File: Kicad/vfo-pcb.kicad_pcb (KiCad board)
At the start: 2 copper layers, 108.3 x 82.9 mm, 66 parts, among them J10 Link-out 1a, J11 RxTx, J13 Link-out 1b, J14 V12, J17 Link-out 2a, J18 Link-out 3, J19 Link-out 2b, J2 Conn_01x07_Female, J3 Si5351, J4 ESP32L, J5 ESP32R, J6 Rotery Encoder1, J7 ILI9341, J8 Rotery Encoder2, J9 Analog in 3-6, SW1 Rotary_Encoder_Switch, U1 AS179-92LF, U2 74HC595, U3 L7805, U4 AS179-92LF

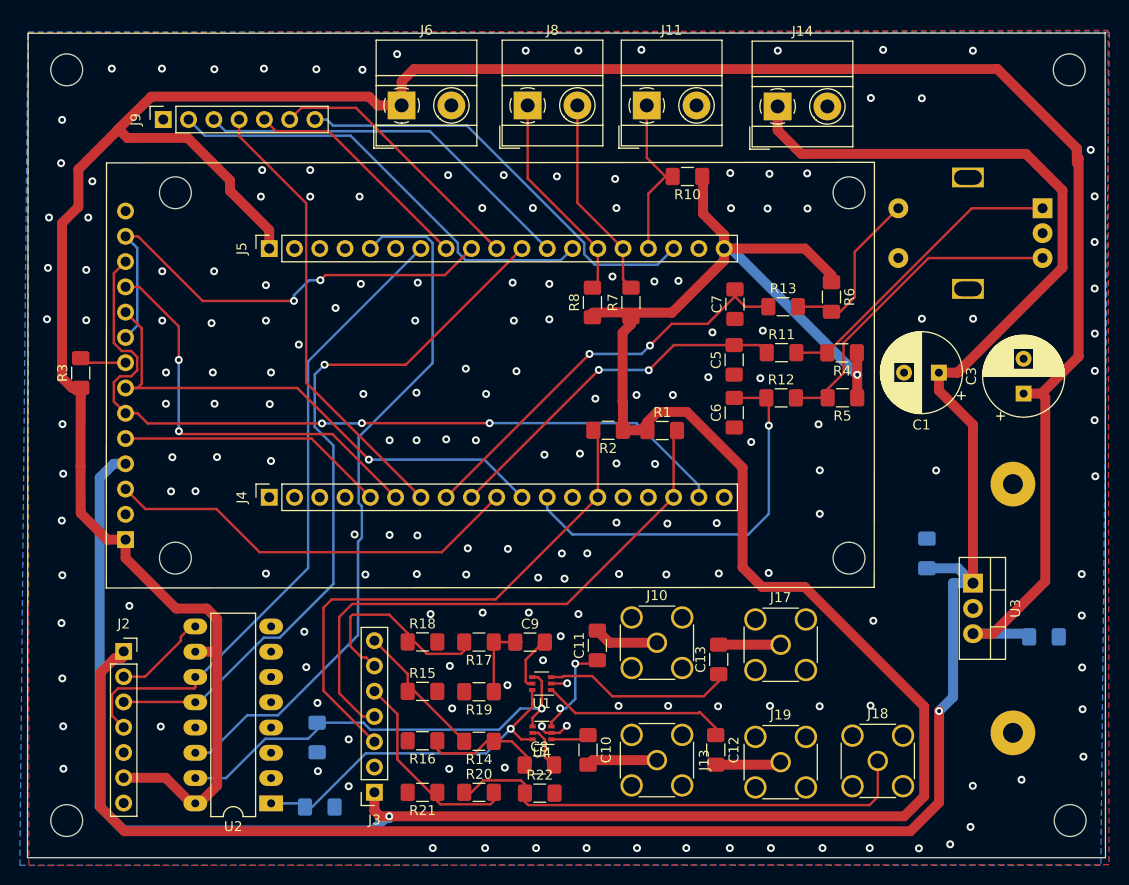
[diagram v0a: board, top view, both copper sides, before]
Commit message: Attenuator removed
To improve crosstalk the attenuators are removed and replaced by 100nF DC blocker
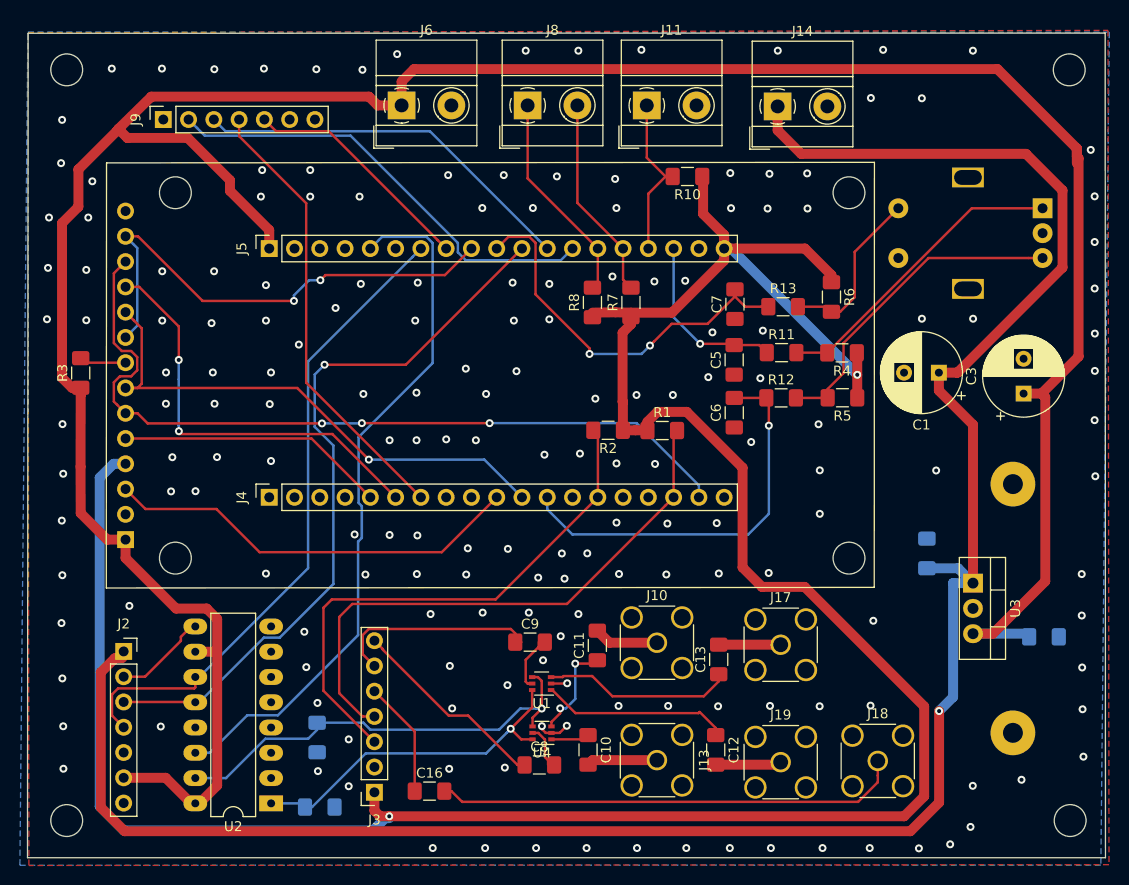
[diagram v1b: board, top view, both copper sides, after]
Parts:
- removed R14, R17, R20: 71, Resistor_SMD:R_1206_3216Metric_Pad1.42x1.75mm_HandSolder
- removed R15, R16, R18, R19, R21, R22: 100, Resistor_SMD:R_1206_3216Metric_Pad1.42x1.75mm_HandSolder
- added C16: 100n, Capacitor_SMD:C_1206_3216Metric_Pad1.42x1.75mm_HandSolder, F.Cu at (82.7, 128.5)
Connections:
- C8 pad 1: Net-(C8-Pad1) -> I3_1
- C9 pad 1: Net-(C9-Pad1) -> I2_1
- J4 pad 8: R3_2a -> Net-(J4-Pad8)
- J4 pad 9: R1_2a -> Net-(J4-Pad9)
- J5 pad 10: A5P -> R3_2a
- J5 pad 17: A6P -> R1_2a
- J9 pad 6: A5P -> Net-(J9-Pad6)
- J9 pad 7: A6P -> Net-(J9-Pad7)
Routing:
- net A6P: track 43.4 -> 0.00 mm
- net A5P: track 27.2 -> 0.00 mm
- net R1_2a: track 36.4 -> 17.7 mm, vias 2 -> 1
- net Net-(C8-Pad1): track 12.2 -> 0.00 mm
- net I1_1: track 20.9 -> 11.7 mm
- net Net-(C9-Pad1): track 7.76 -> 0.00 mm
- net I3_1: track 14.3 -> 20.3 mm
- net R3_2a: track 41.9 -> 39.5 mm
- net Net-(C16-Pad2): track 48.1 -> 47.0 mm
- net I2_1: track 20.9 -> 20.2 mm

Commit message: Add files via upload
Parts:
- removed J17: Link-out 2a, Connector_Coaxial:SMA_Amphenol_132134_Vertical
- removed J18: Link-out 3, Connector_Coaxial:SMA_Amphenol_132134_Vertical
- removed J19: Link-out 2b, Connector_Coaxial:SMA_Amphenol_132134_Vertical
- removed the J9 at (56.0, 61.0)
- removed the U1 at (94.0, 117.7)
- added C17: 100n, Capacitor_SMD:C_1206_3216Metric_Pad1.42x1.75mm_HandSolder, F.Cu at (65.2, 84.3)
- added C18: 100n, Capacitor_SMD:C_1206_3216Metric_Pad1.42x1.75mm_HandSolder, F.Cu at (99.8, 116.3)
- added C19: 100n, Capacitor_SMD:C_1206_3216Metric_Pad1.42x1.75mm_HandSolder, F.Cu at (57.6, 115.9)
- added C20: 100n, Capacitor_SMD:C_1206_3216Metric_Pad1.42x1.75mm_HandSolder, F.Cu at (76.1, 126.2)
- added C21: 100n, Capacitor_SMD:C_1206_3216Metric_Pad1.42x1.75mm_HandSolder, F.Cu at (117.5, 125.9)
- added C22: 100n, Capacitor_SMD:C_1206_3216Metric_Pad1.42x1.75mm_HandSolder, F.Cu at (63.0, 126.0)
- added C23: 100n, Capacitor_SMD:C_1206_3216Metric_Pad1.42x1.75mm_HandSolder, F.Cu at (103.5, 125.9)
- added J11: Link-out 1-1, Connector_Coaxial:SMA_Amphenol_132134_Vertical, F.Cu at (110.9, 127.6)
- added J12: Link-out 1-2, Connector_Coaxial:SMA_Amphenol_132134_Vertical, F.Cu at (97.6, 127.6)
- added J14: Link-out 2-1, Connector_Coaxial:SMA_Amphenol_132134_Vertical, F.Cu at (69.6, 127.6)
- added J15: Link-out 2-2, Connector_Coaxial:SMA_Amphenol_132134_Vertical, F.Cu at (56.2, 127.6)
- added Q1: BFR92, Package_TO_SOT_SMD:SOT-323_SC-70, F.Cu at (75.9, 121.0)
- added Q2: BFR92, Package_TO_SOT_SMD:SOT-323_SC-70, F.Cu at (59.3, 121.7)
- added Q3: BFR92, Package_TO_SOT_SMD:SOT-323_SC-70, F.Cu at (67.6, 117.0)
- added Q4: BFR92, Package_TO_SOT_SMD:SOT-323_SC-70, F.Cu at (120.8, 121.0)
- added Q5: BFR92, Package_TO_SOT_SMD:SOT-323_SC-70, F.Cu at (100.5, 120.7)
- added Q6: BFR92, Package_TO_SOT_SMD:SOT-323_SC-70, F.Cu at (115.3, 121.1)
- added R13: 2.2k, Resistor_SMD:R_1206_3216Metric_Pad1.42x1.75mm_HandSolder, F.Cu at (76.3, 104.4)
- added R14: 2.2k, Resistor_SMD:R_1206_3216Metric_Pad1.42x1.75mm_HandSolder, F.Cu at (69.7, 104.4)
- added R15: 1k, Resistor_SMD:R_1206_3216Metric_Pad1.42x1.75mm_HandSolder, F.Cu at (73.6, 110.0)
- added R16: 1k, Resistor_SMD:R_1206_3216Metric_Pad1.42x1.75mm_HandSolder, F.Cu at (66.5, 112.3)
- added R17: 1k, Resistor_SMD:R_1206_3216Metric_Pad1.42x1.75mm_HandSolder, F.Cu at (60.1, 119.1)
- added R18: 47, Resistor_SMD:R_1206_3216Metric_Pad1.42x1.75mm_HandSolder, F.Cu at (78.4, 116.7)
- added R19: 47, Resistor_SMD:R_1206_3216Metric_Pad1.42x1.75mm_HandSolder, F.Cu at (54.5, 119.4)
- added R20: 47, Resistor_SMD:R_1206_3216Metric_Pad1.42x1.75mm_HandSolder, F.Cu at (64.0, 117.3)
- added R21: 1k, Resistor_SMD:R_1206_3216Metric_Pad1.42x1.75mm_HandSolder, F.Cu at (117.8, 112.7)
- added R22: 1k, Resistor_SMD:R_1206_3216Metric_Pad1.42x1.75mm_HandSolder, F.Cu at (113.2, 112.7)
- added R23: 1k, Resistor_SMD:R_1206_3216Metric_Pad1.42x1.75mm_HandSolder, F.Cu at (108.5, 115.6)
- added R24: 47, Resistor_SMD:R_1206_3216Metric_Pad1.42x1.75mm_HandSolder, F.Cu at (126.1, 115.9)
- added R25: 47, Resistor_SMD:R_1206_3216Metric_Pad1.42x1.75mm_HandSolder, F.Cu at (95.1, 117.6)
- added R26: 47, Resistor_SMD:R_1206_3216Metric_Pad1.42x1.75mm_HandSolder, F.Cu at (110.1, 118.8)
- added U3: Si5351A-B-GT, Package_SO:MSOP-10_3x3mm_P0.5mm, F.Cu at (59.9, 112.7)
- added Y1: Crystal, Crystal:Crystal_SMD_TXC_7M-4Pin_3.2x2.5mm_HandSoldering, F.Cu at (97.4, 110.4)
- added Y2: Crystal, Crystal:Crystal_SMD_TXC_7M-4Pin_3.2x2.5mm_HandSoldering, F.Cu at (50.6, 114.6)
- C14, C15: moved to F.Cu
- C16: value 100n -> 10u
- J10: value Link-out 1a -> Link-out 1-0
- J13: value Link-out 1b -> Link-out 2-0
- J3: value Si5351 -> Analog in 3-6
- R6: renamed from R3; moved to B.Cu
- U2: value 74HC595 -> Si5351A-B-GT; footprint Package_DIP:DIP-16_W7.62mm_LongPads -> Package_SO:MSOP-10_3x3mm_P0.5mm
- U4: value AS179-92LF -> AMS1117; footprint Package_TO_SOT_SMD:SOT-363_SC-70-6 -> Package_TO_SOT_SMD:SOT-223-3_TabPin2
- moved J3 59.7 mm to (74.8, 69.0), turned to 90 degrees
- moved J9 52.7 mm to (57.7, 62.0), turned to 90 degrees
- moved C16 51.7 mm to (65.2, 79.8), turned to 180 degrees
- moved U4 44.3 mm to (63.6, 90.4), turned to 0 degrees
- moved C13 44.1 mm to (68.0, 121.0), turned to 0 degrees
- moved U2 42.1 mm to (104.8, 111.7), turned to 0 degrees
- moved C9 40.4 mm to (52.5, 110.2)
- moved C10 27.7 mm to (126.1, 120.4), turned to 0 degrees
- moved J13 22.7 mm to (83.0, 127.6), turned to 0 degrees
- moved J10 22.6 mm to (123.3, 127.6)
- moved C8 21.1 mm to (102.6, 106.7), turned to 270 degrees
- moved C15 17.0 mm to (54.5, 122.0), turned to 180 degrees
- moved C12 16.7 mm to (95.1, 120.8), turned to 180 degrees
- moved C14 13.3 mm to (81.5, 121.1)
- moved C11 13.2 mm to (110.0, 121.9), turned to 180 degrees
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- renumbered C5 to C3, C3 to C4, C6 to C5, C4 to C6, J6 to J1, J8 to J2, J11 to J4, J14 to J5, J4 to J6, J5 to J7, J7 to J8, J2 to J9, R7 to R1, R12 to R10, R6 to R11, R13 to R12, R8 to R2, R10 to R3, R1 to R4, R2 to R5, R4 to R7, R11 to R8, R5 to R9, U3 to U1
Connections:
- C14 pad 1: Qb -> Net-(C14-Pad1)
- C14 pad 2: GND -> Net-(C14-Pad2)
- C15 pad 1: Qa -> Net-(C15-Pad1)
- C15 pad 2: GND -> Net-(C15-Pad2)
- C16 pad 1: I1_1 -> V33a
- C16 pad 2: Net-(C16-Pad2) -> GND
- C8 pad 1: I3_1 -> GND
- C8 pad 2: Net-(C8-Pad2) -> V33a
- C9 pad 1: I2_1 -> GND
- C9 pad 2: Net-(C9-Pad2) -> V33a
- J10 pad 1: Net-(C11-Pad2) -> Net-(C10-Pad2)
- J13 pad 1: Net-(C10-Pad2) -> Net-(C14-Pad2)
- J3 pad 1: V33 -> GND
- J3 pad 2: GND -> A1P
- J3 pad 3: SDA_1 -> A2P
- J3 pad 4: SCL_1 -> A3P
- J3 pad 5: I1_1 -> A4P
- J3 pad 6: I2_1 -> Net-(J3-Pad6)
- J3 pad 7: I3_1 -> Net-(J3-Pad7)
- J6 pad 8: Net-(J4-Pad8) -> SDA_2
- J6 pad 9: Net-(J4-Pad9) -> SCL_2
- J8 pad 4: V33 -> V33a
- J9 pad 2: Dout -> SER_2
- U2 pad 1: Qb -> V33a
- U2 pad 10: Vcc -> Net-(R21-Pad2)
- U2 pad 4: Net-(U2-Pad4) -> SCL_1
- U2 pad 5: Net-(U2-Pad5) -> SDA_1
- U2 pad 7: Net-(U2-Pad7) -> V33a
- U2 pad 9: Dout -> Net-(R22-Pad2)
- U4 pad 1: Net-(C10-Pad1) -> GND
- U4 pad 2: GND -> V33a
- U4 pad 3: Net-(C11-Pad1) -> Vcc
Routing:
- net V33a: track 0.00 -> 292.4 mm, vias 0 -> 4
- net V33: track 256.9 -> 75.6 mm, vias 2 -> 1
- net V12V: track 214.0 -> 150.4 mm, vias 1 -> 0
- net SER_2: track 71.0 -> 21.5 mm
- net SCL_2: track 0.00 -> 48.0 mm, vias 0 -> 1
- net Net-(C16-Pad2): track 47.0 -> 0.00 mm
- net Qa: track 44.8 -> 0.00 mm, vias 1 -> 0
- net SCLK_2: track 66.2 -> 21.5 mm
- net RCLK_2: track 73.9 -> 35.7 mm, vias 1 -> 0
- net SDA_2: track 0.00 -> 37.4 mm, vias 0 -> 1
- net Qb: track 34.9 -> 0.00 mm, vias 1 -> 0
- net SCL_1: track 57.6 -> 23.2 mm
- net A1P: track 45.5 -> 24.2 mm
- net I3_1: track 20.3 -> 0.00 mm
- net I2_1: track 20.2 -> 0.00 mm
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
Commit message: Add files via upload
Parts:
- removed C10, C11, C12, C13, C14, C15: 100n, Capacitor_SMD:C_1206_3216Metric_Pad1.42x1.75mm_HandSolder
- Q1, Q2, Q3, Q4, Q5, Q6: footprint Package_TO_SOT_SMD:SOT-323_SC-70 -> Package_TO_SOT_SMD:SOT-23
- R18, R19, R20, R24, R25: value 47 -> 20
- moved R20 6.01 mm to (68.1, 121.7), turned to 0 degrees
- moved R18 5.88 mm to (81.5, 121.7), turned to 0 degrees
- moved R24 5.84 mm to (125.9, 121.8), turned to 0 degrees
- moved R25 4.02 mm to (95.5, 121.6), turned to 180 degrees
- moved R26 3.25 mm to (110.4, 122.1), turned to 180 degrees
- moved R19 1.70 mm to (54.2, 121.1), turned to 270 degrees
- moved J15 0.70 mm to (56.1, 128.3)
- moved J10 0.70 mm to (123.3, 128.3)
- moved J11 0.70 mm to (110.9, 128.3)
- moved J12 0.70 mm to (97.6, 128.3)
- moved J13 0.70 mm to (83.0, 128.3)
- moved J14 0.70 mm to (69.6, 128.3)
- moved R17 0.64 mm to (59.8, 118.5)
- moved Y2 0.57 mm to (50.7, 115.1), turned to 180 degrees
- moved Y1 0.41 mm to (97.7, 110.6), turned to 180 degrees
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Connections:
- J10 pad 1: Net-(C10-Pad2) -> Net-(J10-Pad1)
- J11 pad 1: Net-(C11-Pad2) -> Net-(J11-Pad1)
- J12 pad 1: Net-(C12-Pad2) -> Net-(J12-Pad1)
- J13 pad 1: Net-(C14-Pad2) -> Net-(J13-Pad1)
- J14 pad 1: Net-(C13-Pad2) -> Net-(J14-Pad1)
- J15 pad 1: Net-(C15-Pad2) -> Net-(J15-Pad1)
- Q1 pad 2: Net-(C14-Pad1) -> Net-(Q1-Pad2)
- Q2 pad 2: Net-(C15-Pad1) -> Net-(Q2-Pad2)
- Q3 pad 2: Net-(C13-Pad1) -> Net-(Q3-Pad2)
- Q4 pad 2: Net-(C10-Pad1) -> Net-(Q4-Pad2)
- Q5 pad 2: Net-(C12-Pad1) -> Net-(Q5-Pad2)
- Q6 pad 2: Net-(C11-Pad1) -> Net-(Q6-Pad2)
- R18 pad 1: GND -> Net-(Q1-Pad2)
- R18 pad 2: Net-(C14-Pad1) -> Net-(J13-Pad1)
- R19 pad 1: GND -> Net-(Q2-Pad2)
- R19 pad 2: Net-(C15-Pad1) -> Net-(J15-Pad1)
- R20 pad 1: GND -> Net-(Q3-Pad2)
- R20 pad 2: Net-(C13-Pad1) -> Net-(J14-Pad1)
- R24 pad 1: GND -> Net-(Q4-Pad2)
- R24 pad 2: Net-(C10-Pad1) -> Net-(J10-Pad1)
- R25 pad 1: GND -> Net-(Q5-Pad2)
- R25 pad 2: Net-(C12-Pad1) -> Net-(J12-Pad1)
- R26 pad 1: GND -> Net-(Q6-Pad2)
- R26 pad 2: Net-(C11-Pad1) -> Net-(J11-Pad1)
- Y1 pad 1: Net-(U2-Pad3) -> Net-(U2-Pad2)
- Y1 pad 2: Net-(U2-Pad2) -> GND
- Y1 pad 3: (no net) -> Net-(U2-Pad3)
- Y2 pad 1: Net-(U3-Pad3) -> Net-(U3-Pad2)
- Y2 pad 2: Net-(U3-Pad2) -> GND
- Y2 pad 3: (no net) -> Net-(U3-Pad3)
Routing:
- net Net-(C13-Pad1): track 9.76 -> 0.00 mm
- net Net-(C10-Pad2): track 9.61 -> 0.00 mm
- net Net-(C12-Pad2): track 9.10 -> 0.00 mm
- net Net-(J10-Pad1): track 0.00 -> 8.66 mm
- net Net-(J12-Pad1): track 0.00 -> 8.61 mm
- net Net-(J11-Pad1): track 0.00 -> 7.45 mm
- net Net-(C15-Pad2): track 7.33 -> 0.00 mm
- net Net-(C10-Pad1): track 7.26 -> 0.00 mm
- net Net-(C14-Pad1): track 7.04 -> 0.00 mm
- net Net-(C11-Pad2): track 6.68 -> 0.00 mm
- net Net-(C13-Pad2): track 6.63 -> 0.00 mm
- net Net-(J14-Pad1): track 0.00 -> 6.62 mm
- net Net-(J13-Pad1): track 0.00 -> 6.60 mm
- net Net-(C12-Pad1): track 6.59 -> 0.00 mm
- net Net-(J15-Pad1): track 0.00 -> 6.51 mm
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
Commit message: Add files via upload
Updated output circuit added pi attenuation
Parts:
- added R19: 1k, Resistor_SMD:R_1206_3216Metric_Pad1.42x1.75mm_HandSolder, F.Cu at (114.8, 112.6)
- added R21: 150, Resistor_SMD:R_1206_3216Metric_Pad1.42x1.75mm_HandSolder, F.Cu at (81.5, 117.7)
- added R23: 150, Resistor_SMD:R_1206_3216Metric_Pad1.42x1.75mm_HandSolder, F.Cu at (124.5, 113.0)
- added R24: 150, Resistor_SMD:R_1206_3216Metric_Pad1.42x1.75mm_HandSolder, F.Cu at (100.9, 118.9)
- added R25: 150, Resistor_SMD:R_1206_3216Metric_Pad1.42x1.75mm_HandSolder, F.Cu at (67.1, 119.3)
- added R29: 150, Resistor_SMD:R_1206_3216Metric_Pad1.42x1.75mm_HandSolder, F.Cu at (108.2, 118.6)
- added R32: 150, Resistor_SMD:R_1206_3216Metric_Pad1.42x1.75mm_HandSolder, F.Cu at (127.5, 118.7)
- added R33: 150, Resistor_SMD:R_1206_3216Metric_Pad1.42x1.75mm_HandSolder, F.Cu at (81.5, 114.3)
- added R34: 150, Resistor_SMD:R_1206_3216Metric_Pad1.42x1.75mm_HandSolder, F.Cu at (63.2, 128.3)
- added R36: 150, Resistor_SMD:R_1206_3216Metric_Pad1.42x1.75mm_HandSolder, F.Cu at (102.5, 124.0)
- added R37: 150, Resistor_SMD:R_1206_3216Metric_Pad1.42x1.75mm_HandSolder, F.Cu at (76.3, 127.2)
- added R38: 150, Resistor_SMD:R_1206_3216Metric_Pad1.42x1.75mm_HandSolder, F.Cu at (105.6, 124.0)
- R22: value 1k -> 150
- R26: renamed from R18; value 20 -> 33
- R27: renamed from R19; value 20 -> 33
- R28: renamed from R24; value 20 -> 33
- R30: renamed from R25; value 20 -> 33
- R31: renamed from R20; value 20 -> 33
- R35: renamed from R26; value 47 -> 33
- moved R22 65.9 mm to (47.8, 120.1), turned to 270 degrees
- moved C7 20.4 mm to (86.7, 114.3), turned to 0 degrees
- moved C16 13.0 mm to (112.2, 112.6)
- moved R20 7.52 mm to (100.9, 116.1)
- moved R26 6.54 mm to (86.7, 117.7)
- moved Q4 6.04 mm to (95.6, 117.0)
- moved C3 5.29 mm to (77.1, 121.0)
- moved Q1 4.95 mm to (75.0, 116.1)
- moved R31 4.76 mm to (72.3, 119.4)
- moved R30 4.54 mm to (91.4, 119.6), turned to 270 degrees
- moved R27 3.98 mm to (50.4, 120.1)
- moved R35 3.54 mm to (111.2, 118.6), turned to 270 degrees
- moved R17 3.54 mm to (63.2, 117.4), turned to 90 degrees
- moved R28 3.40 mm to (124.7, 118.6), turned to 270 degrees
- moved   3.12 mm to (46.0, 128.4)
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- renumbered C16 to C1, C4 to C10, C5 to C11, C6 to C12, C7 to C13, C9 to C14, C8 to C15, C18 to C16, C19 to C17, C17 to C2, C20 to C3, C21 to C4, C22 to C5, C1 to C6, C23 to C7, C2 to C8, C3 to C9, J12 to J10, J10 to J11, J13 to J12, J15 to J13, J11 to J15, Q4 to Q3, Q5 to Q4, Q3 to Q5, R12 to R10, R4 to R11, R13 to R12, R5 to R13, R21 to R18, R23 to R20, R6 to R4, R7 to R5, R8 to R6, R9 to R7, R10 to R8, R11 to R9, U4 to U1, U1 to U2, U2 to U4, Y2 to Y1, Y1 to Y2
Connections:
- R22 pad 1: Net-(Q6-Pad1) -> Net-(Q2-Pad2)
- R22 pad 2: Net-(R22-Pad2) -> GND
- U4 pad 9: Net-(R22-Pad2) -> Net-(R19-Pad2)
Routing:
- net V33a: track 288.5 -> 235.5 mm, vias 2 -> 0
- net Net-(J12-Pad1): track 6.60 -> 18.2 mm
- net Net-(J13-Pad1): track 6.51 -> 16.6 mm
- net Net-(R19-Pad2): track 0.00 -> 9.31 mm
- net SCL_2: track 48.0 -> 39.2 mm, vias 1 -> 2
- net Net-(J14-Pad1): track 6.62 -> 15.2 mm
- net Net-(Q1-Pad2): track 3.84 -> 10.8 mm
- net Net-(R22-Pad2): track 6.94 -> 0.00 mm
- net Net-(Q4-Pad2): track 2.49 -> 8.79 mm
- net Net-(Q2-Pad2): track 5.49 -> 11.5 mm
- net Net-(J10-Pad1): track 8.61 -> 14.4 mm
- net Net-(Q1-Pad1): track 13.1 -> 7.83 mm
- net Net-(Q6-Pad2): track 2.41 -> 7.48 mm
- net Net-(Q4-Pad1): track 9.23 -> 4.85 mm
- net Net-(Q6-Pad1): track 6.96 -> 2.99 mm
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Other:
- board size 108.3 x 82.9 mm -> 108.4 x 79.9 mm
- net class power: clearance 0.5 -> 0.3; trace_width 1 -> 0.5

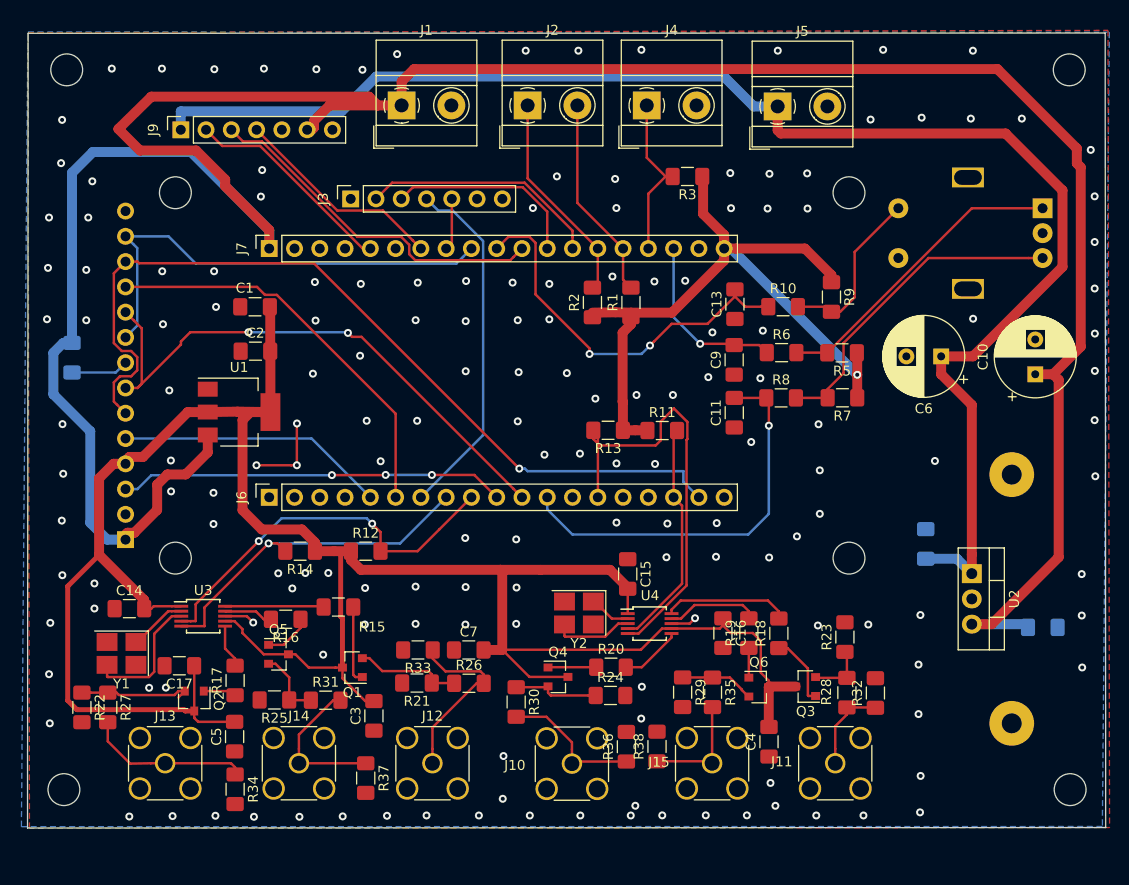
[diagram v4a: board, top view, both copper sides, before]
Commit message: wifi update LM7805 version
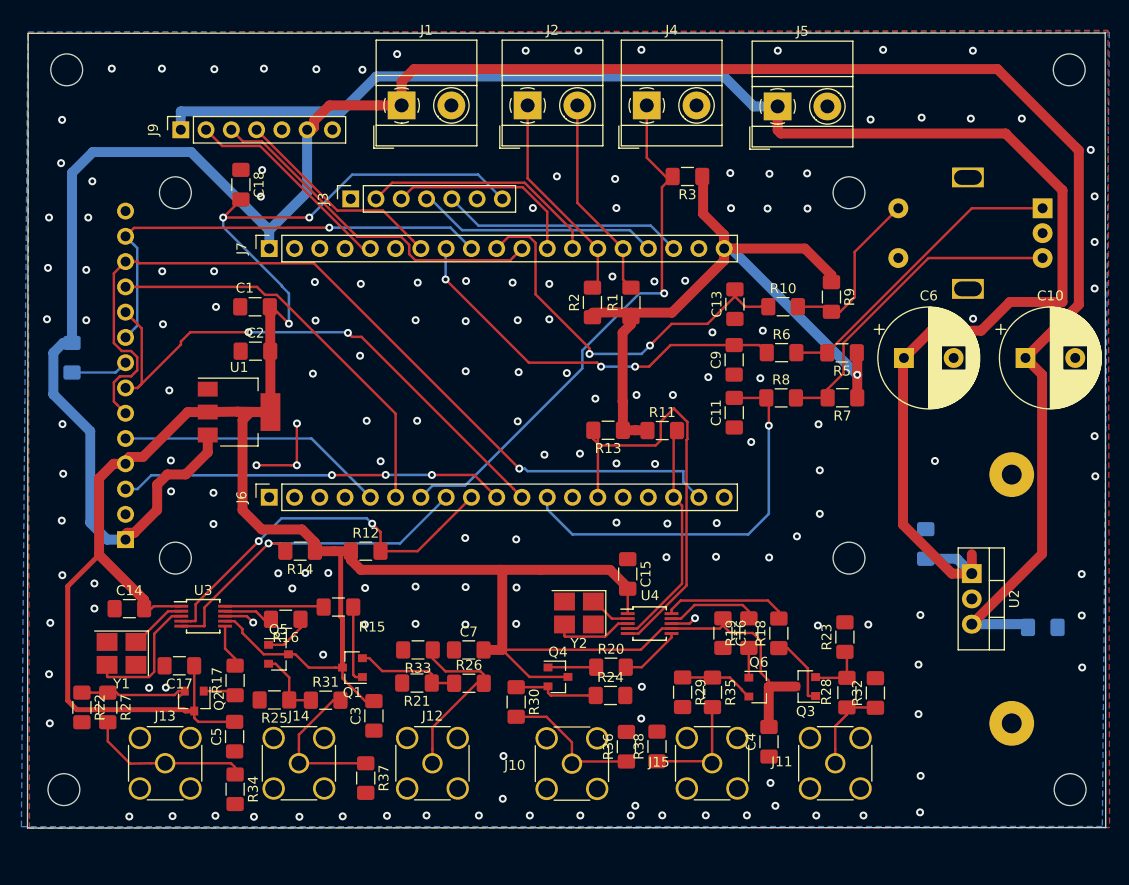
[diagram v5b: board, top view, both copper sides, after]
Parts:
- added C18: 100n, Capacitor_SMD:C_1206_3216Metric_Pad1.42x1.75mm_HandSolder, F.Cu at (63.8, 67.6)
- C10: value 100u -> 2200u; footprint Capacitor_THT:CP_Radial_D8.0mm_P3.50mm -> Capacitor_THT:CP_Radial_D10.0mm_P5.00mm
- C6: value 100u -> 1000u; footprint Capacitor_THT:CP_Radial_D8.0mm_P3.50mm -> Capacitor_THT:CP_Radial_D10.0mm_P5.00mm
- R3: value 2.2k -> 680
- moved C6 3.75 mm to (130.4, 85.0), turned to 0 degrees
- moved C10 1.91 mm to (142.6, 85.0), turned to 0 degrees
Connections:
- J3 pad 7: Net-(J3-Pad7) -> V33a
- J6 pad 7: A3P -> RXTX
- J7 pad 16: RXTX -> A3P
- J7 pad 17: R1_2a -> A4P
- J7 pad 8: A4P -> R1_2a
- SW1 pad MP: (no net) -> GND
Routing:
- net V33a: track 235.5 -> 284.9 mm, vias 0 -> 3
- net Vcc: track 279.5 -> 239.6 mm
- net RXTX: track 16.6 -> 54.9 mm, vias 0 -> 1
- net R1_2a: track 17.7 -> 40.3 mm, vias 1 -> 3
- net A4P: track 5.23 -> 24.4 mm
- net A3P: track 35.8 -> 24.4 mm
- net V12V: track 150.0 -> 160.5 mm
- net SDO: track 47.7 -> 47.2 mm, vias 0 -> 1
- net GND: vias 167 -> 165
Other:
- net class power: trace_width 0.5 -> 1
